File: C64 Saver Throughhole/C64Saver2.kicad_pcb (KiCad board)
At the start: 2 copper layers, 43.9 x 28.8 mm, 24 parts, among them J1 Conn_01x04, J2 Conn_01x08, J4 Conn_01x08, J5 Conn_01x04, J6 Conn_01x04, Q1 BC547, Q2 IRFR5305, U1 TL431LP

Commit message: 2.7 with iBom and gerbers
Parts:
- added R2: 330 1%, Resistor_THT:R_Axial_DIN0204_L3.6mm_D1.6mm_P5.08mm_Horizontal, F.Cu at (172.7, 93.7)
- LED1: footprint LED_THT:LED_D3.0mm -> LED_THT:LED_D3.0mm_Easy_1
- LED2: footprint LED_THT:LED_D3.0mm -> LED_THT:LED_D3.0mm_Easy_2
- Q1, U1: footprint Package_TO_SOT_THT:TO-92_Inline -> Package_TO_SOT_THT:TO-92_Inline_Wide
- Q2: value IRFR5305 -> IPD068P03L3G
- R10: value 1k -> 330
- R3: renamed from R1; value 3k9 1% -> 3k3 1%
- moved R5 14.3 mm to (175.1, 89.3)
- moved R4 7.78 mm to (175.1, 91.6), turned to 180 degrees
- moved R3 6.13 mm to (170.4, 93.7)
- moved LED2 5.38 mm to (162.7, 98.0), turned to 180 degrees
- moved R1 5.18 mm to (175.0, 98.8)
- moved U1 5.02 mm to (166.9, 102.7), turned to 180 degrees
- moved C1 4.52 mm to (173.9, 103.4)
- moved LED1 4.43 mm to (165.4, 98.0)
- moved Z1 3.56 mm to (149.9, 107.6)
- moved R11 3.56 mm to (152.9, 107.6)
- moved Q1 3.40 mm to (156.9, 100.2), turned to -90 degrees
- moved R6 2.40 mm to (167.7, 89.2)
- moved R10 0.49 mm to (151.4, 97.5)
- moved R8 0.06 mm to (163.0, 89.2)
- renumbered R2 to R1, R7 to R11, R5 to R4, R9 to R5, R3 to R6, R8 to R7, R4 to R8, R6 to R9
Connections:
- LED2 pad 2: /VCC1- -> /5V_SAFE
- R10 pad 2: OVERVOLTAGE -> GND
- R3 pad 2: /SENSE -> unconnected-(R3-Pad2)
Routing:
- net GND: track 32.0 -> 0.19 mm
- net PGATE: track 32.6 -> 49.4 mm, vias 1 -> 0
- net /9VAC1: track 23.9 -> 34.5 mm
- net /NGATE: track 12.7 -> 20.7 mm
- net /9VAC1': track 16.9 -> 24.6 mm
- net /5V_SAFE: track 0.00 -> 7.61 mm
- net /9VAC2: track 50.2 -> 43.2 mm
- net OVERVOLTAGE: track 37.9 -> 33.8 mm, vias 1 -> 0
- net Net-(LED1-K): track 12.2 -> 15.1 mm
- net /SENSE: track 23.1 -> 25.6 mm
- net /VCC1-: track 84.0 -> 84.9 mm
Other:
- rule pad_to_mask_clearance: 0.2 -> 0
- board text added: "C64 Saver 2 THT version Rev 2.7 BWACK, Everlast 2023"
- board text added: "GRN"
- board text added: "RED"
- board text removed: "C64 Saver 2 THT version Rev 2.6 BWACK 2023"

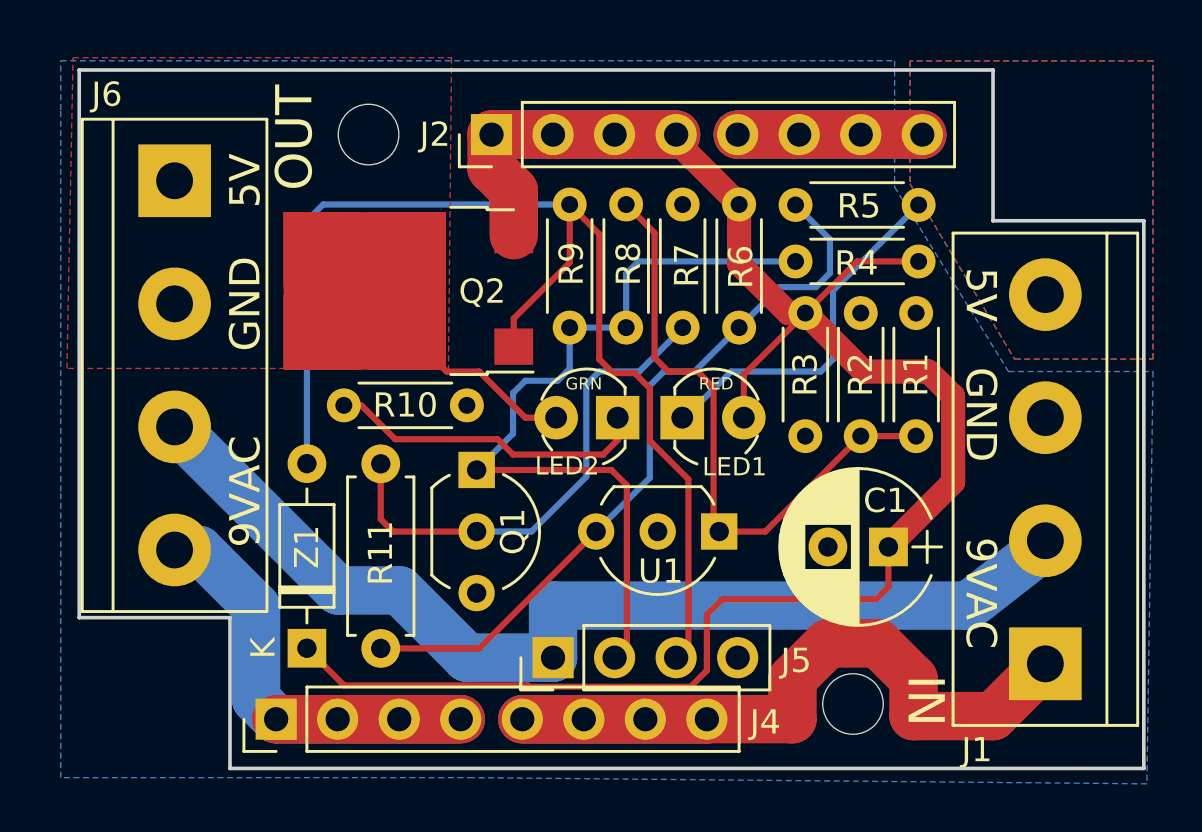
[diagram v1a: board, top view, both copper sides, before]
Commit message: Updates to both kicad and easyeda versions. I found a missing connection in the earlier untested Kicad version. :(
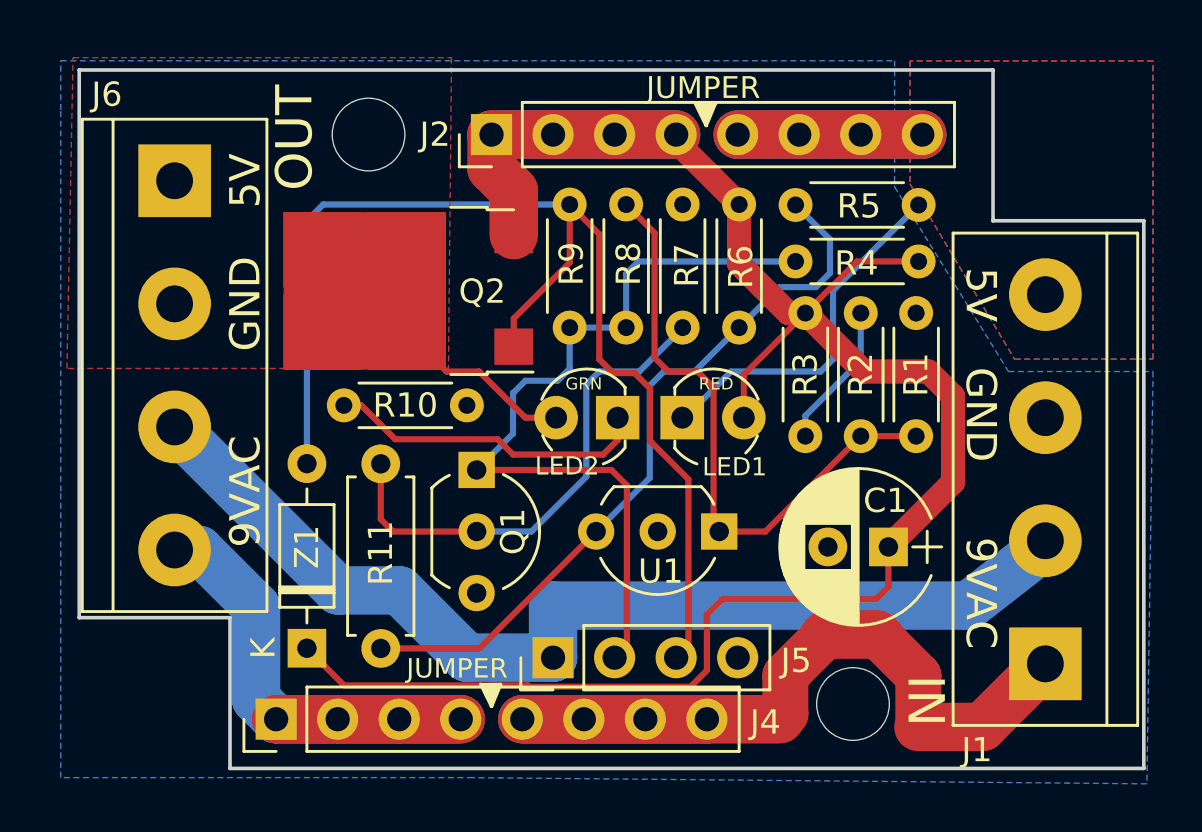
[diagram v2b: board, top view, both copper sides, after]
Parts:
- R2: value 330 1% -> 510 1%
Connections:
- net /9VAC1' renamed /9VAC1B
- R2 pad 1: unconnected-(R2-Pad1) -> /DIVIDER
- R3 pad 2: unconnected-(R3-Pad2) -> /DIVIDER
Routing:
- net /DIVIDER: track 0.00 -> 6.03 mm
- net /9VAC1: track 34.5 -> 35.5 mm
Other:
- board text added: "JUMPER"
